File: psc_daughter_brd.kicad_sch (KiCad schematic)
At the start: 4 parts

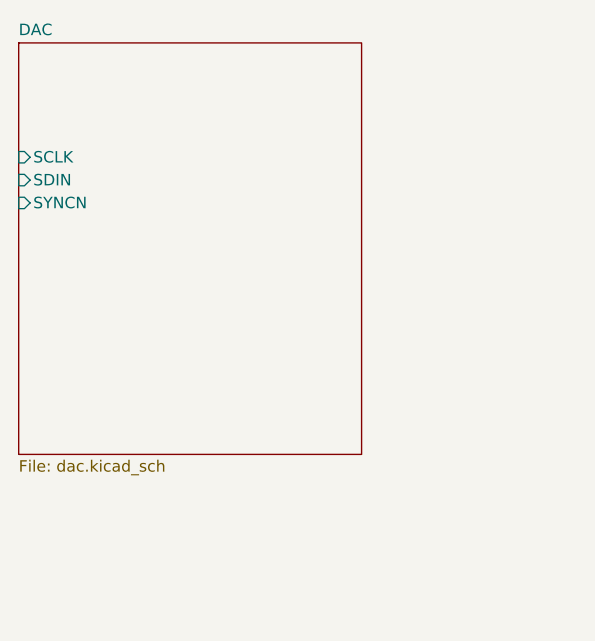
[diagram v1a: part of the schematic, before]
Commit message: Add ADR1001 Voltage Reference
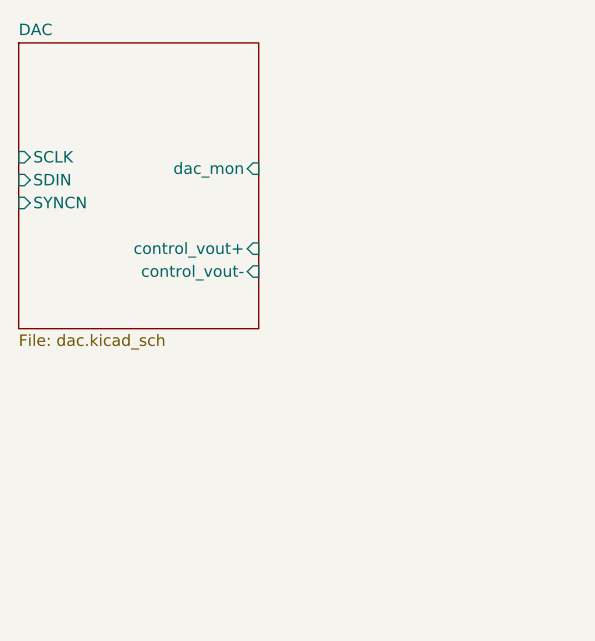
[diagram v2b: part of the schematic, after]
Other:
- sheet DAC ports: added control_vout+, control_vout-, dac_mon; removed none
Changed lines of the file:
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@@
 	(sheet
 		(at 80.01 72.39)
-		(size 38.1 45.72)
+		(size 26.67 31.75)
 		(exclude_from_sim no)
 		(in_bom yes)
@@
 		)
 		(fill
-			(color 0 0 0 0.0000)
+			(color 157 202 145 0.8700)
 		)
 		(property "Sheetname" "DAC"
@@
 		)
 		(property "Sheetfile" "dac.kicad_sch"
-			(at 80.01 118.6946 0)
+			(at 80.01 104.7246 0)
 			(effects
 				(font
@@
 			)
 		)
+		(pin "control_vout+" input
+			(at 106.68 95.25 0)
+			(effects
+				(font
+					(size 1.27 1.27)
+				)
+				(justify right)
+			)
+		)
+		(pin "control_vout-" input
+			(at 106.68 97.79 0)
+			(effects
+				(font
+					(size 1.27 1.27)
+				)
+				(justify right)
+			)
+		)
+		(pin "dac_mon" input
+			(at 106.68 86.36 0)
+			(effects
+				(font
+					(size 1.27 1.27)
+				)
+				(justify right)
+			)
+		)

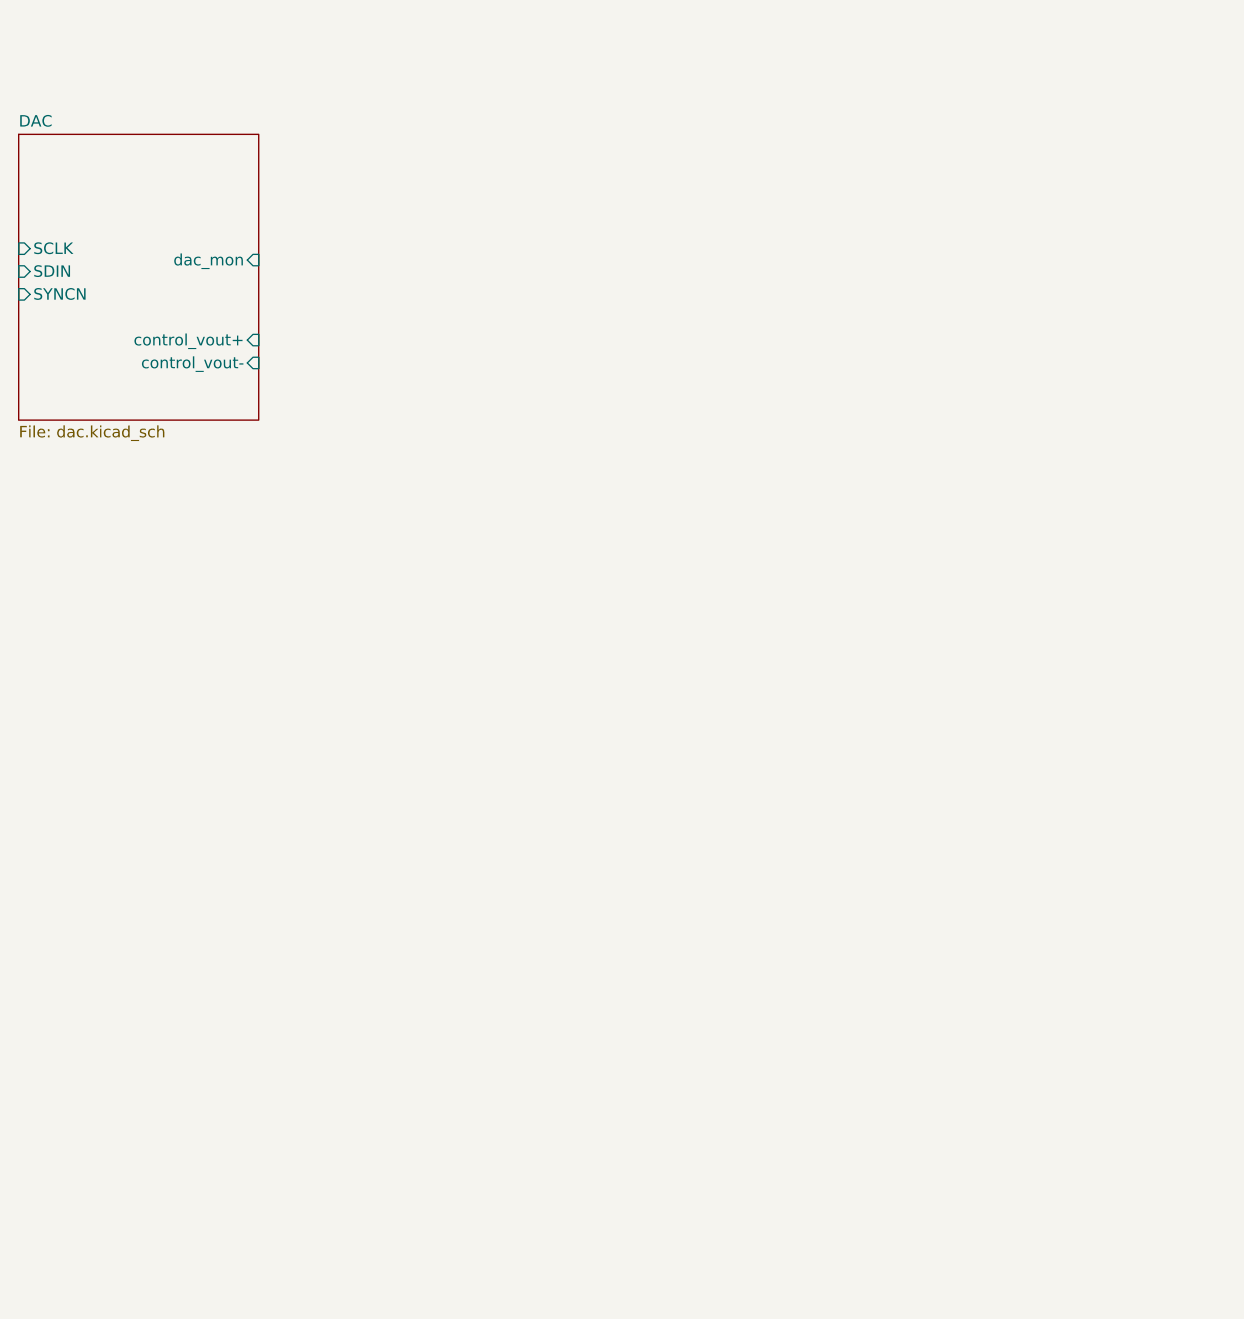
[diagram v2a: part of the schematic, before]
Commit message: Add ADC monitor circuit
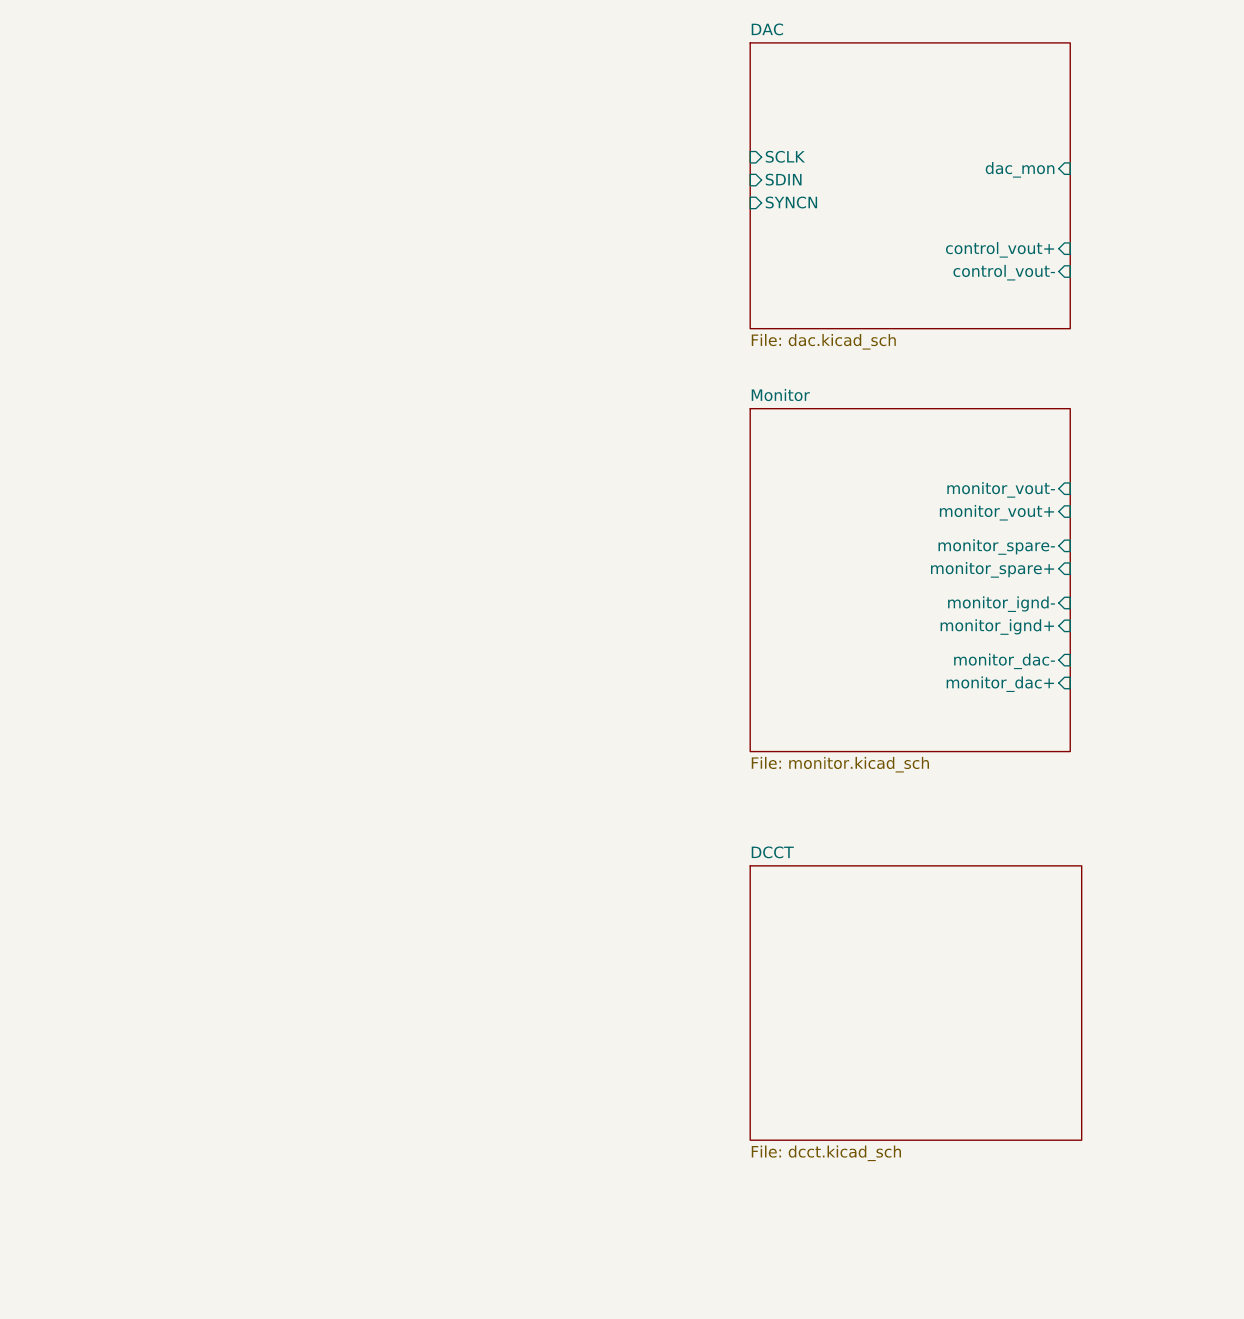
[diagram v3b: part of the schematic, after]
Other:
- added sheet DCCT (dcct.kicad_sch)
- added sheet Monitor (monitor.kicad_sch)
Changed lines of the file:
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@@
 	)
 	(sheet
-		(at 80.01 72.39)
-		(size 26.67 31.75)
+		(at 161.29 102.87)
+		(size 35.56 38.1)
 		(exclude_from_sim no)
 		(in_bom yes)
@@
 		)
 		(fill
-			(color 157 202 145 0.8700)
+			(color 255 255 194 1.0000)
+		)
+		(property "Sheetname" "Monitor"
+			(at 161.29 102.1584 0)
+			(effects
+				(font
+					(size 1.27 1.27)
+				)
+				(justify left bottom)
+			)
+		)
+		(property "Sheetfile" "monitor.kicad_sch"
+			(at 161.29 141.5546 0)
+			(effects
+				(font
+					(size 1.27 1.27)
+				)
+				(justify left top)
+			)
+		)
+		(pin "monitor_dac+" input
+			(at 196.85 133.35 0)
+			(effects
+				(font
+					(size 1.27 1.27)
+				)
+				(justify right)
+			)
+		)
+		(pin "monitor_dac-" input
+			(at 196.85 130.81 0)
+			(effects
+				(font
+					(size 1.27 1.27)
+				)
+				(justify right)
+			)
+		)
+		(pin "monitor_ignd+" input
+			(at 196.85 127 0)
+			(effects
+				(font
+					(size 1.27 1.27)
+				)
+				(justify right)
+			)
+		)
+		(pin "monitor_ignd-" input
+			(at 196.85 124.46 0)
+			(effects
+				(font
+					(size 1.27 1.27)
+				)
+				(justify right)
+			)
+		)
+		(pin "monitor_spare+" input
+			(at 196.85 120.65 0)
+			(effects
+				(font
+					(size 1.27 1.27)
+				)
+				(justify right)
+			)
+		)
+		(pin "monitor_spare-" input
+			(at 196.85 118.11 0)
+			(effects
+				(font
+					(size 1.27 1.27)
+				)
+				(justify right)
+			)
+		)
+		(pin "monitor_vout+" input
+			(at 196.85 114.3 0)
+			(effects
+				(font
+					(size 1.27 1.27)
+				)
+				(justify right)
+			)
+		)
+		(pin "monitor_vout-" input
+			(at 196.85 111.76 0)
+			(effects
+				(font
+					(size 1.27 1.27)
+				)
+				(justify right)
+			)
+		)
+		(instances
+			(project "psc_daughter_brd"
+				(path "/40891cc8-bf64-41f4-8f69-a607d7b280eb"
+					(page "4")
+				)
+			)
+		)
+	)
+	(sheet
+		(at 161.29 153.67)
+		(size 36.83 30.48)
+		(exclude_from_sim no)
+		(in_bom yes)
+		(on_board yes)
+		(dnp no)
+		(fields_autoplaced yes)
+		(stroke
+			(width 0.1524)
+			(type solid)
+		)
+		(fill
+			(color 255 255 194 1.0000)
+		)
+		(property "Sheetname" "DCCT"
+			(at 161.29 152.9584 0)
+			(effects
+				(font
+					(size 1.27 1.27)
+				)
+				(justify left bottom)
+			)
+		)
+		(property "Sheetfile" "dcct.kicad_sch"
+			(at 161.29 184.7346 0)
+			(effects
+				(font
+					(size 1.27 1.27)
+				)
+				(justify left top)
+			)
+		)
+		(instances
+			(project "psc_daughter_brd"
+				(path "/40891cc8-bf64-41f4-8f69-a607d7b280eb"
+					(page "5")
+				)
+			)
+		)
+	)
+	(sheet
+		(at 161.29 62.23)
+		(size 35.56 31.75)
+		(exclude_from_sim no)
+		(in_bom yes)
+		(on_board yes)
+		(dnp no)
+		(fields_autoplaced yes)
+		(stroke
+			(width 0.1524)
+			(type solid)
+		)
+		(fill
+			(color 255 255 194 1.0000)
 		)
 		(property "Sheetname" "DAC"
-			(at 80.01 71.6784 0)
+			(at 161.29 61.5184 0)
 			(effects
 				(font
@@
 		)
 		(property "Sheetfile" "dac.kicad_sch"
-			(at 80.01 104.7246 0)
+			(at 161.29 94.5646 0)
 			(effects
 				(font
@@
 		)
 		(pin "SCLK" input
-			(at 80.01 85.09 180)
+			(at 161.29 74.93 180)
 			(effects
 				(font
@@
 		)
 		(pin "SDIN" input
-			(at 80.01 87.63 180)
+			(at 161.29 77.47 180)
 			(effects
 				(font
@@
 		)
 		(pin "SYNCN" input
-			(at 80.01 90.17 180)
+			(at 161.29 80.01 180)
 			(effects
 				(font
@@
 		)
 		(pin "control_vout+" input
-			(at 106.68 95.25 0)
+			(at 196.85 85.09 0)
 			(effects
 				(font
@@
 		)
 		(pin "control_vout-" input
-			(at 106.68 97.79 0)
+			(at 196.85 87.63 0)
 			(effects
 				(font
@@
 		)
 		(pin "dac_mon" input
-			(at 106.68 86.36 0)
-			(effects
-				(font
+			(at 196.85 76.2 0)
+			(effects
+				(font

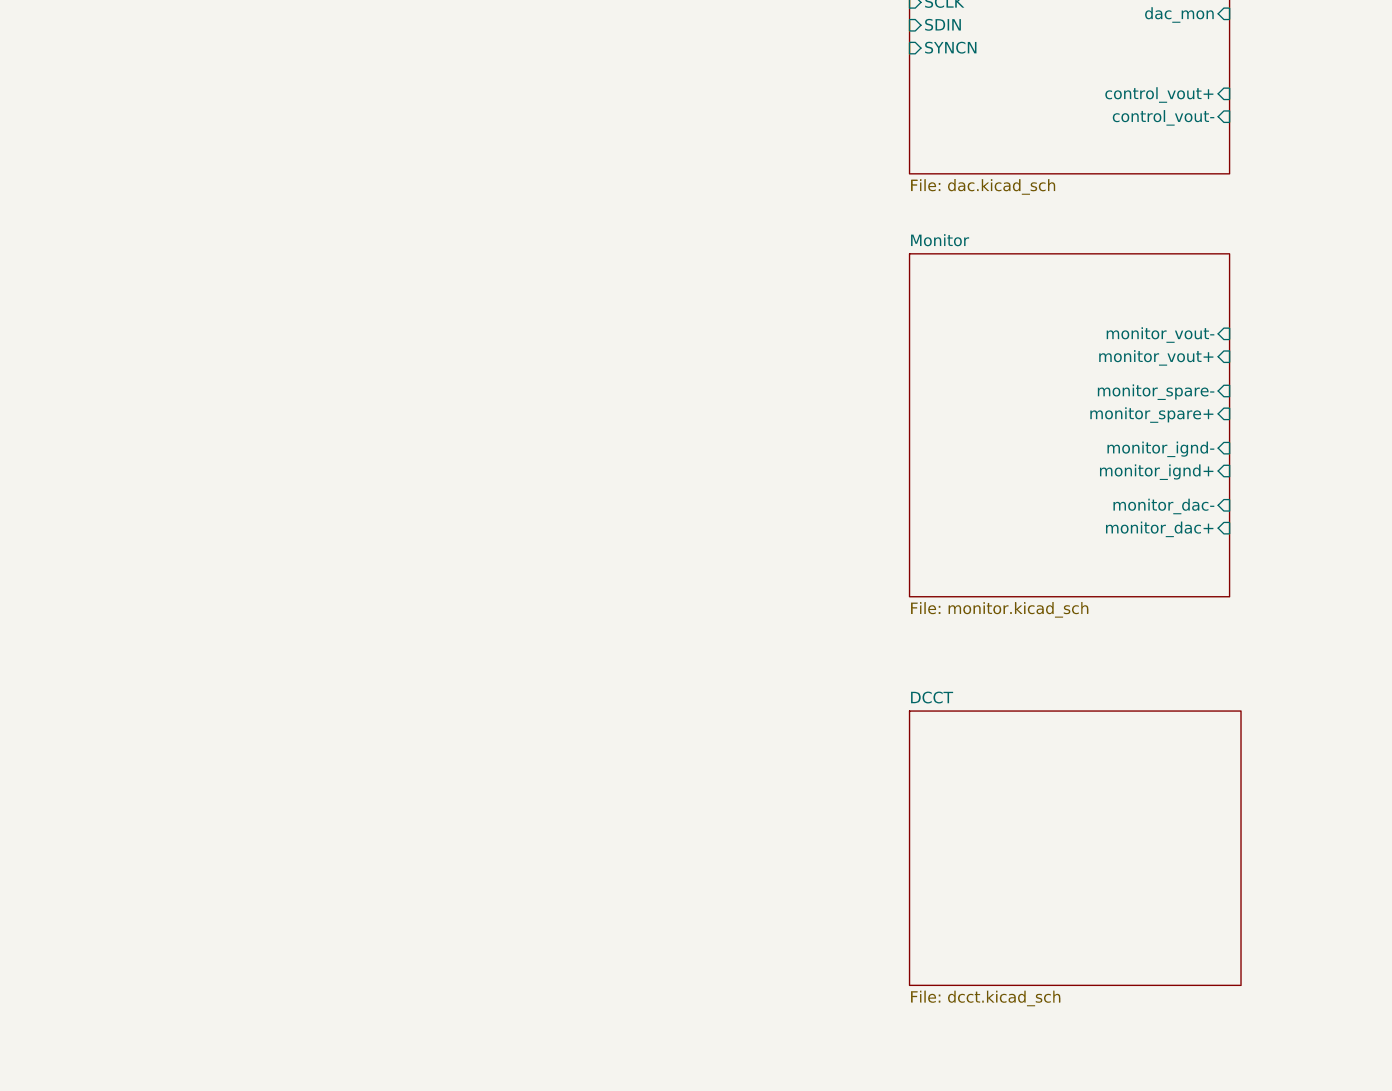
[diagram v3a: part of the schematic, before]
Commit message: Change board size, add DB connector
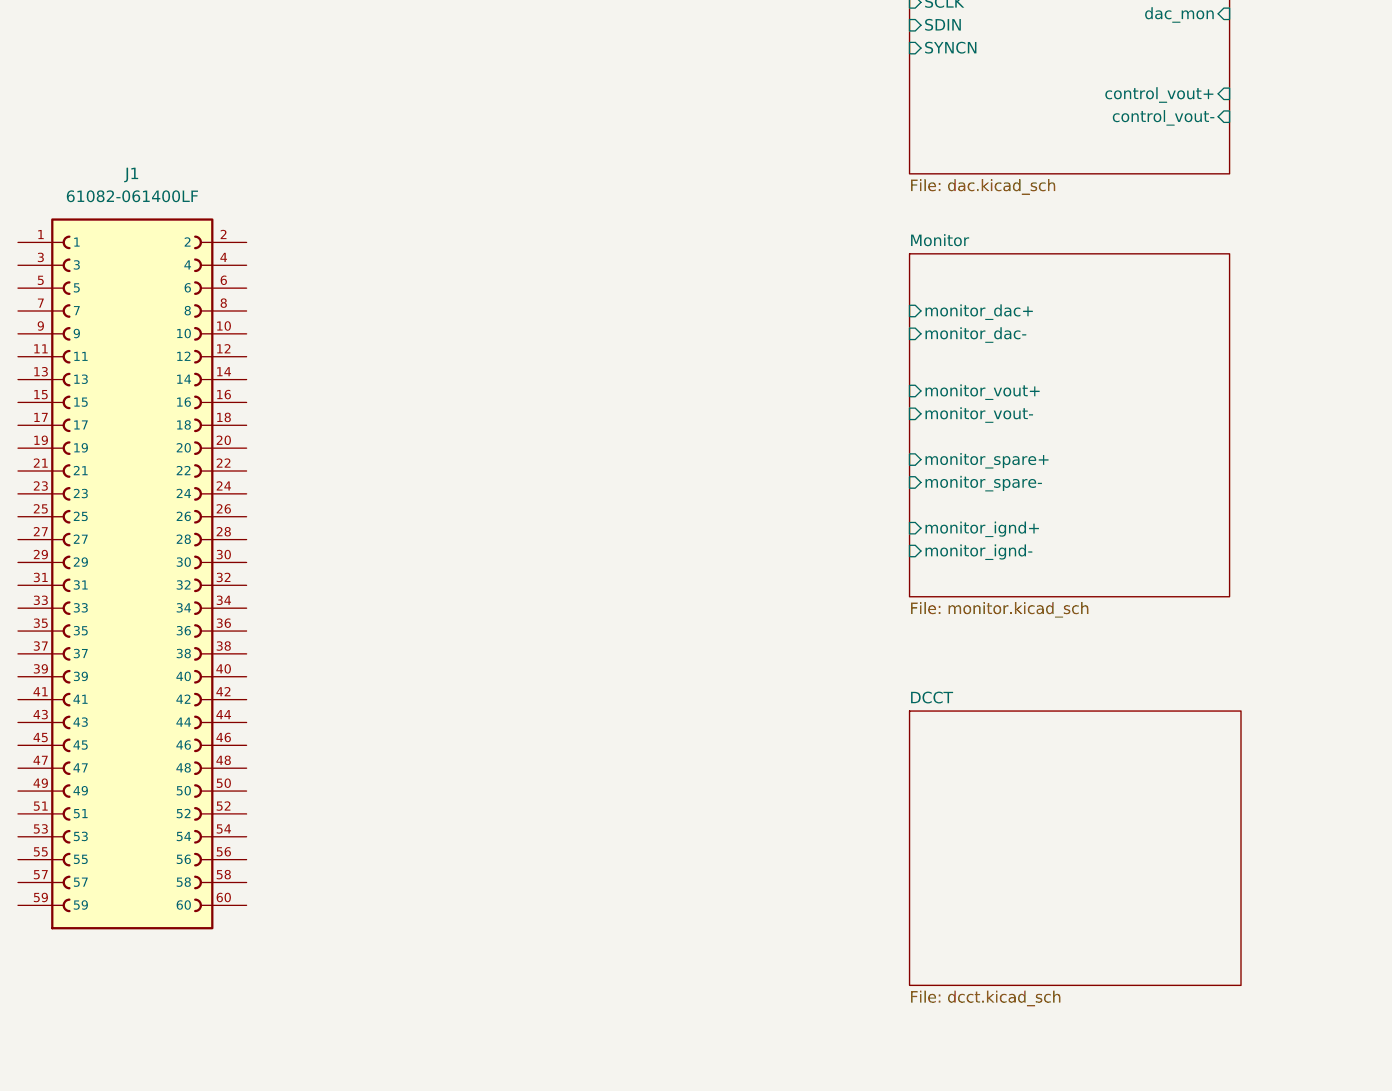
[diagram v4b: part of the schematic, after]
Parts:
- added J1: 61082-061400LF, myparts:AMPHENOL_61082-061400LF, symbol PSC:61082-061400LF
- MT1, MT2, MT3, MT4: footprint MountingHole:MountingHole_4.3mm_M4_DIN965_Pad -> MountingHole:MountingHole_3.2mm_M3_Pad_TopBottom
